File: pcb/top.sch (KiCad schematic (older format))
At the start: 12 parts, among them J11 1-MALE, J12 1-FEMALE, J13 2-MALE, J14 2-FEMALE, J15 3-MALE, J16 3-FEMALE, J17 4-MALE, J18 4-FEMALE, SW1 ACTION, SW2 ACTION, SW3 ACTION, SW4 ACTION

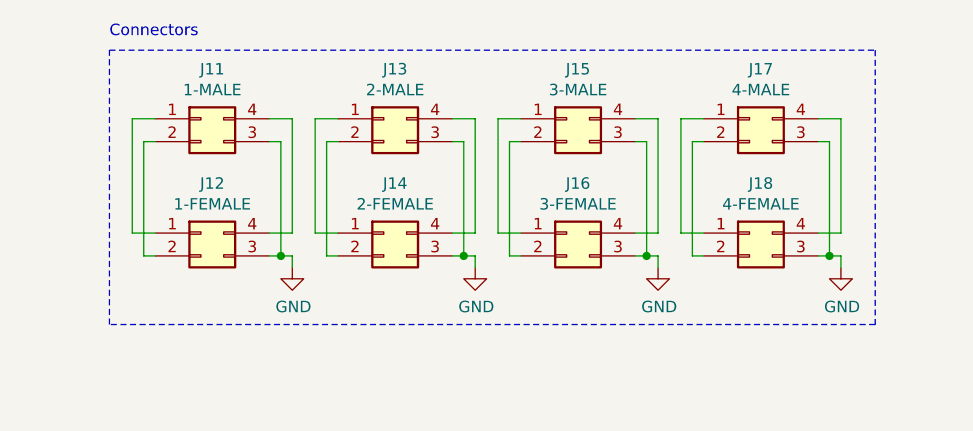
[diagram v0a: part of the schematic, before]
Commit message: Assign footprints and complete BOM
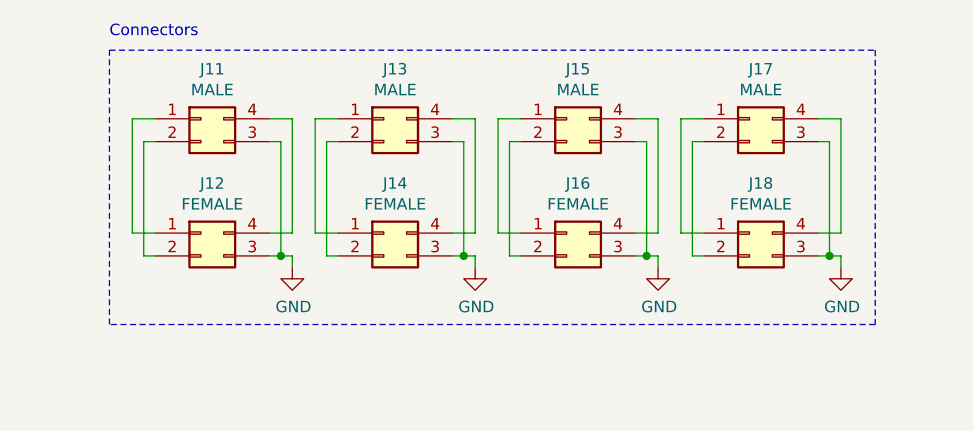
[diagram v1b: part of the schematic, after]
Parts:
- J11: value 1-MALE -> MALE; LCSC Part # (none) -> C239333; MPN (none) -> A2541WR-2x2P; Manufacturer (none) -> CJT(Changjiang Connectors)
- J12: value 1-FEMALE -> FEMALE; LCSC Part # (none) -> C239353; MPN (none) -> A2541HWR-2x2P; Manufacturer (none) -> CJT(Changjiang Connectors)
- J13: value 2-MALE -> MALE; LCSC Part # (none) -> C239333; MPN (none) -> A2541WR-2x2P; Manufacturer (none) -> CJT(Changjiang Connectors)
- J14: value 2-FEMALE -> FEMALE; LCSC Part # (none) -> C239353; MPN (none) -> A2541HWR-2x2P; Manufacturer (none) -> CJT(Changjiang Connectors)
- J15: value 3-MALE -> MALE; LCSC Part # (none) -> C239333; MPN (none) -> A2541WR-2x2P; Manufacturer (none) -> CJT(Changjiang Connectors)
- J16: value 3-FEMALE -> FEMALE; LCSC Part # (none) -> C239353; MPN (none) -> A2541HWR-2x2P; Manufacturer (none) -> CJT(Changjiang Connectors)
- J17: value 4-MALE -> MALE; LCSC Part # (none) -> C239333; MPN (none) -> A2541WR-2x2P; Manufacturer (none) -> CJT(Changjiang Connectors)
- J18: value 4-FEMALE -> FEMALE; LCSC Part # (none) -> C239353; MPN (none) -> A2541HWR-2x2P; Manufacturer (none) -> CJT(Changjiang Connectors)
- SW1, SW2, SW3, SW4: footprint (none) -> Button_Switch_SMD:SW_SPST_TL3305A; LCSC Part # (none) -> C412374; MPN (none) -> TS4560TP; Manufacturer (none) -> SHOU HAN
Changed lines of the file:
@@
 AR Path="/5C920CA4/5F6ACD6B" Ref="J11"  Part="1"
 F 0 "J11" H 3850 2317 50  0000 C CNN
-F 1 "1-MALE" H 3850 2226 50  0000 C CNN
+F 1 "MALE" H 3850 2226 50  0000 C CNN
 F 2 "Connector_PinHeader_2.54mm:PinHeader_2x02_P2.54mm_Horizontal" H 3800 2100 50  0001 C CNN
-F 3 "~" H 3800 2100 50  0001 C CNN
+F 3 "https://datasheet.lcsc.com/szlcsc/2008120037_CJT-Changjiang-Connectors-A2541WR-2x2P_C239333.pdf" H 3800 2100 50  0001 C CNN
+F 4 "C239333" H 3800 2100 50  0001 C CNN "LCSC Part #"
+F 5 "A2541WR-2x2P" H 3800 2100 50  0001 C CNN "MPN"
+F 6 "CJT(Changjiang Connectors)" H 3800 2100 50  0001 C CNN "Manufacturer"
 	1    3800 2100
 	1    0    0    -1
@@
 AR Path="/5C920CA4/5F6ACD85" Ref="J12"  Part="1"
 F 0 "J12" H 3850 2817 50  0000 C CNN
-F 1 "1-FEMALE" H 3850 2726 50  0000 C CNN
+F 1 "FEMALE" H 3850 2726 50  0000 C CNN
 F 2 "Connector_PinSocket_2.54mm:PinSocket_2x02_P2.54mm_Horizontal" H 3800 2600 50  0001 C CNN
-F 3 "~" H 3800 2600 50  0001 C CNN
+F 3 "https://datasheet.lcsc.com/szlcsc/2008120038_CJT-Changjiang-Connectors-A2541HWR-2x2P_C239353.pdf" H 3800 2600 50  0001 C CNN
+F 4 "C239353" H 3800 2600 50  0001 C CNN "LCSC Part #"
+F 5 "A2541HWR-2x2P" H 3800 2600 50  0001 C CNN "MPN"
+F 6 "CJT(Changjiang Connectors)" H 3800 2600 50  0001 C CNN "Manufacturer"
 	1    3800 2600
 	1    0    0    -1
@@
 AR Path="/5C920CA4/5F6B6610" Ref="J13"  Part="1"
 F 0 "J13" H 4650 2317 50  0000 C CNN
-F 1 "2-MALE" H 4650 2226 50  0000 C CNN
+F 1 "MALE" H 4650 2226 50  0000 C CNN
 F 2 "Connector_PinHeader_2.54mm:PinHeader_2x02_P2.54mm_Horizontal" H 4600 2100 50  0001 C CNN
-F 3 "~" H 4600 2100 50  0001 C CNN
+F 3 "https://datasheet.lcsc.com/szlcsc/2008120037_CJT-Changjiang-Connectors-A2541WR-2x2P_C239333.pdf" H 4600 2100 50  0001 C CNN
+F 4 "C239333" H 4600 2100 50  0001 C CNN "LCSC Part #"
+F 5 "A2541WR-2x2P" H 4600 2100 50  0001 C CNN "MPN"
+F 6 "CJT(Changjiang Connectors)" H 4600 2100 50  0001 C CNN "Manufacturer"
 	1    4600 2100
 	1    0    0    -1
@@
 AR Path="/5C920CA4/5F6B6626" Ref="J14"  Part="1"
 F 0 "J14" H 4650 2817 50  0000 C CNN
-F 1 "2-FEMALE" H 4650 2726 50  0000 C CNN
+F 1 "FEMALE" H 4650 2726 50  0000 C CNN
 F 2 "Connector_PinSocket_2.54mm:PinSocket_2x02_P2.54mm_Horizontal" H 4600 2600 50  0001 C CNN
-F 3 "~" H 4600 2600 50  0001 C CNN
+F 3 "https://datasheet.lcsc.com/szlcsc/2008120038_CJT-Changjiang-Connectors-A2541HWR-2x2P_C239353.pdf" H 4600 2600 50  0001 C CNN
+F 4 "C239353" H 4600 2600 50  0001 C CNN "LCSC Part #"
+F 5 "A2541HWR-2x2P" H 4600 2600 50  0001 C CNN "MPN"
+F 6 "CJT(Changjiang Connectors)" H 4600 2600 50  0001 C CNN "Manufacturer"
 	1    4600 2600
 	1    0    0    -1
@@
 AR Path="/5C920CA4/5F6B83E3" Ref="J15"  Part="1"
 F 0 "J15" H 5450 2317 50  0000 C CNN
-F 1 "3-MALE" H 5450 2226 50  0000 C CNN
+F 1 "MALE" H 5450 2226 50  0000 C CNN
 F 2 "Connector_PinHeader_2.54mm:PinHeader_2x02_P2.54mm_Horizontal" H 5400 2100 50  0001 C CNN
-F 3 "~" H 5400 2100 50  0001 C CNN
+F 3 "https://datasheet.lcsc.com/szlcsc/2008120037_CJT-Changjiang-Connectors-A2541WR-2x2P_C239333.pdf" H 5400 2100 50  0001 C CNN
+F 4 "C239333" H 5400 2100 50  0001 C CNN "LCSC Part #"
+F 5 "A2541WR-2x2P" H 5400 2100 50  0001 C CNN "MPN"
+F 6 "CJT(Changjiang Connectors)" H 5400 2100 50  0001 C CNN "Manufacturer"
 	1    5400 2100
 	1    0    0    -1
@@
 AR Path="/5C920CA4/5F6B83F9" Ref="J16"  Part="1"
 F 0 "J16" H 5450 2817 50  0000 C CNN
-F 1 "3-FEMALE" H 5450 2726 50  0000 C CNN
+F 1 "FEMALE" H 5450 2726 50  0000 C CNN
 F 2 "Connector_PinSocket_2.54mm:PinSocket_2x02_P2.54mm_Horizontal" H 5400 2600 50  0001 C CNN
-F 3 "~" H 5400 2600 50  0001 C CNN
+F 3 "https://datasheet.lcsc.com/szlcsc/2008120038_CJT-Changjiang-Connectors-A2541HWR-2x2P_C239353.pdf" H 5400 2600 50  0001 C CNN
+F 4 "C239353" H 5400 2600 50  0001 C CNN "LCSC Part #"
+F 5 "A2541HWR-2x2P" H 5400 2600 50  0001 C CNN "MPN"
+F 6 "CJT(Changjiang Connectors)" H 5400 2600 50  0001 C CNN "Manufacturer"
 	1    5400 2600
 	1    0    0    -1
@@
 AR Path="/5C920CA4/5F6BA361" Ref="J17"  Part="1"
 F 0 "J17" H 6250 2317 50  0000 C CNN
-F 1 "4-MALE" H 6250 2226 50  0000 C CNN
+F 1 "MALE" H 6250 2226 50  0000 C CNN
 F 2 "Connector_PinHeader_2.54mm:PinHeader_2x02_P2.54mm_Horizontal" H 6200 2100 50  0001 C CNN
-F 3 "~" H 6200 2100 50  0001 C CNN
+F 3 "https://datasheet.lcsc.com/szlcsc/2008120037_CJT-Changjiang-Connectors-A2541WR-2x2P_C239333.pdf" H 6200 2100 50  0001 C CNN
+F 4 "C239333" H 6200 2100 50  0001 C CNN "LCSC Part #"
+F 5 "A2541WR-2x2P" H 6200 2100 50  0001 C CNN "MPN"
+F 6 "CJT(Changjiang Connectors)" H 6200 2100 50  0001 C CNN "Manufacturer"
 	1    6200 2100
 	1    0    0    -1
@@
 AR Path="/5C920CA4/5F6BA377" Ref="J18"  Part="1"
 F 0 "J18" H 6250 2817 50  0000 C CNN
-F 1 "4-FEMALE" H 6250 2726 50  0000 C CNN
+F 1 "FEMALE" H 6250 2726 50  0000 C CNN
 F 2 "Connector_PinSocket_2.54mm:PinSocket_2x02_P2.54mm_Horizontal" H 6200 2600 50  0001 C CNN
-F 3 "~" H 6200 2600 50  0001 C CNN
+F 3 "https://datasheet.lcsc.com/szlcsc/2008120038_CJT-Changjiang-Connectors-A2541HWR-2x2P_C239353.pdf" H 6200 2600 50  0001 C CNN
+F 4 "C239353" H 6200 2600 50  0001 C CNN "LCSC Part #"
+F 5 "A2541HWR-2x2P" H 6200 2600 50  0001 C CNN "MPN"
+F 6 "CJT(Changjiang Connectors)" H 6200 2600 50  0001 C CNN "Manufacturer"
 	1    6200 2600
 	1    0    0    -1
@@
 F 0 "SW1" H 2900 4485 50  0000 C CNN
 F 1 "ACTION" H 2900 4394 50  0000 C CNN
-F 2 "" H 2900 4400 50  0001 C CNN
-F 3 "~" H 2900 4400 50  0001 C CNN
+F 2 "Button_Switch_SMD:SW_SPST_TL3305A" H 2900 4400 50  0001 C CNN
+F 3 "https://datasheet.lcsc.com/szlcsc/1912111437_SHOU-HAN-TS4560TP_C412374.pdf" H 2900 4400 50  0001 C CNN
+F 4 "C412374" H 2900 4200 50  0001 C CNN "LCSC Part #"
+F 5 "TS4560TP" H 2900 4200 50  0001 C CNN "MPN"
+F 6 "SHOU HAN" H 2900 4200 50  0001 C CNN "Manufacturer"
 	1    2900 4200
 	1    0    0    -1
@@
 F 0 "SW2" H 4400 4485 50  0000 C CNN
 F 1 "ACTION" H 4400 4394 50  0000 C CNN
-F 2 "" H 4400 4400 50  0001 C CNN
-F 3 "~" H 4400 4400 50  0001 C CNN
+F 2 "Button_Switch_SMD:SW_SPST_TL3305A" H 4400 4400 50  0001 C CNN
+F 3 "https://datasheet.lcsc.com/szlcsc/1912111437_SHOU-HAN-TS4560TP_C412374.pdf" H 4400 4400 50  0001 C CNN
+F 4 "C412374" H 4400 4200 50  0001 C CNN "LCSC Part #"
+F 5 "TS4560TP" H 4400 4200 50  0001 C CNN "MPN"
+F 6 "SHOU HAN" H 4400 4200 50  0001 C CNN "Manufacturer"
 	1    4400 4200
 	1    0    0    -1
@@
 F 0 "SW3" H 5900 4485 50  0000 C CNN
 F 1 "ACTION" H 5900 4394 50  0000 C CNN
-F 2 "" H 5900 4400 50  0001 C CNN
-F 3 "~" H 5900 4400 50  0001 C CNN
+F 2 "Button_Switch_SMD:SW_SPST_TL3305A" H 5900 4400 50  0001 C CNN
+F 3 "https://datasheet.lcsc.com/szlcsc/1912111437_SHOU-HAN-TS4560TP_C412374.pdf" H 5900 4400 50  0001 C CNN
+F 4 "C412374" H 5900 4200 50  0001 C CNN "LCSC Part #"
+F 5 "TS4560TP" H 5900 4200 50  0001 C CNN "MPN"
+F 6 "SHOU HAN" H 5900 4200 50  0001 C CNN "Manufacturer"
 	1    5900 4200
 	1    0    0    -1
@@
 F 0 "SW4" H 7400 4485 50  0000 C CNN
 F 1 "ACTION" H 7400 4394 50  0000 C CNN
-F 2 "" H 7400 4400 50  0001 C CNN
-F 3 "~" H 7400 4400 50  0001 C CNN
+F 2 "Button_Switch_SMD:SW_SPST_TL3305A" H 7400 4400 50  0001 C CNN
+F 3 "https://datasheet.lcsc.com/szlcsc/1912111437_SHOU-HAN-TS4560TP_C412374.pdf" H 7400 4400 50  0001 C CNN
+F 4 "C412374" H 7400 4200 50  0001 C CNN "LCSC Part #"
+F 5 "TS4560TP" H 7400 4200 50  0001 C CNN "MPN"
+F 6 "SHOU HAN" H 7400 4200 50  0001 C CNN "Manufacturer"
 	1    7400 4200
 	1    0    0    -1

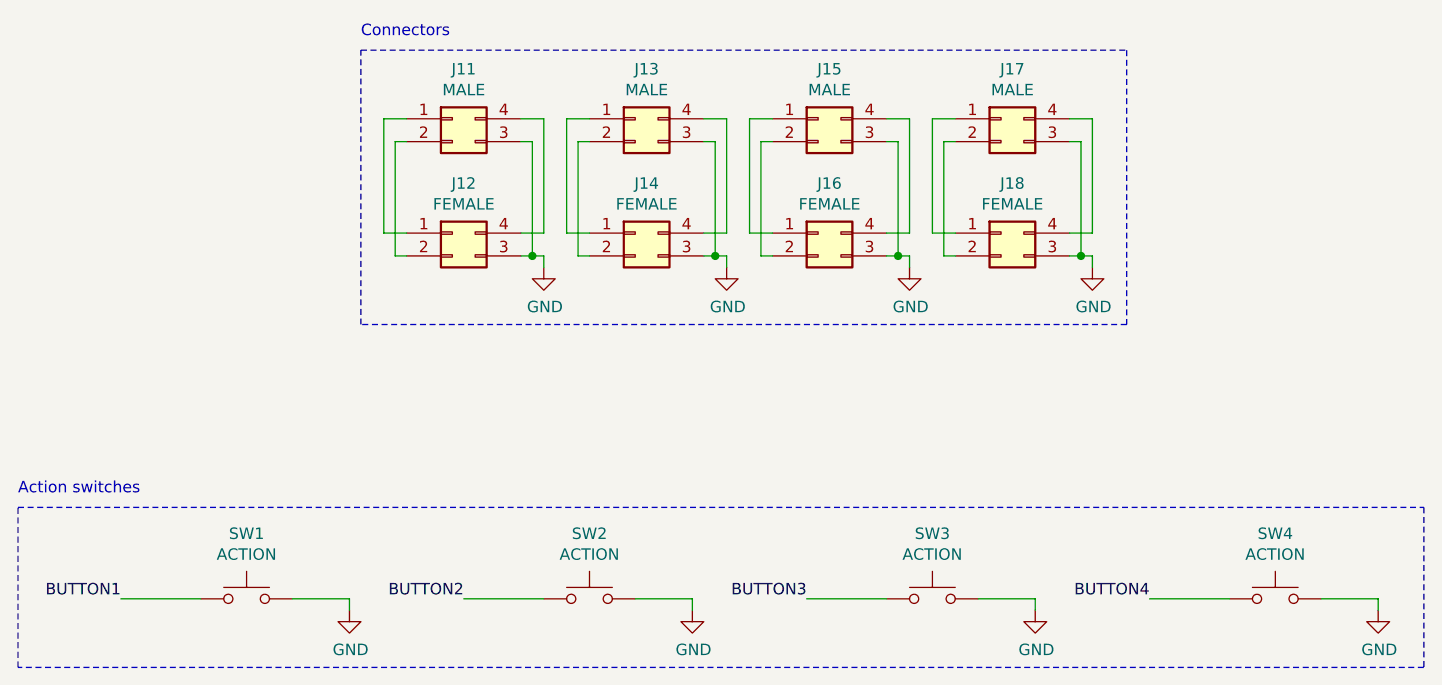
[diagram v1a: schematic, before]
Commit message: Add buzzer and clean up
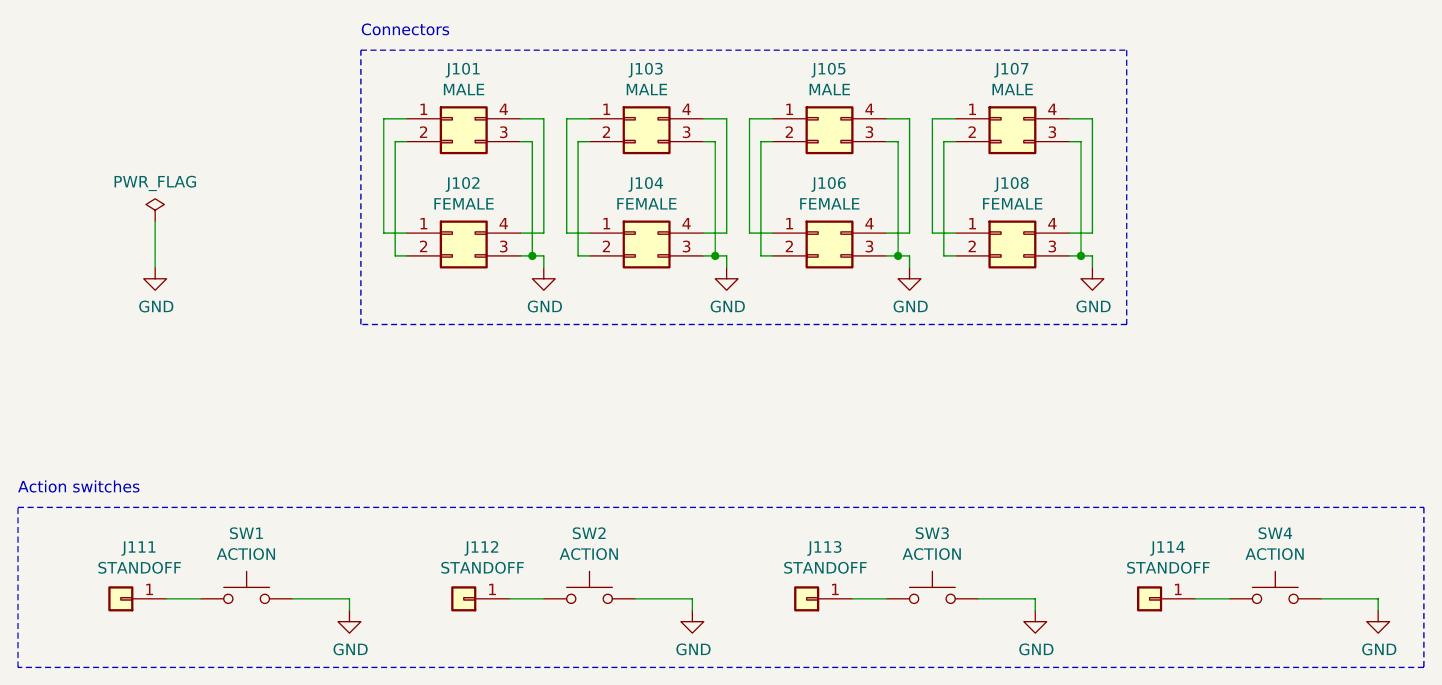
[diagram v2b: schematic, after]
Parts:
- added J111, J112, J113, J114: STANDOFF, MountingHole:MountingHole_2.2mm_M2_Pad_Via, symbol Connector_Generic:Conn_01x01
- renumbered J11 to J101, J12 to J102, J13 to J103, J14 to J104, J15 to J105, J16 to J106, J17 to J107, J18 to J108
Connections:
- net BUTTON1: no longer names the net of SW1.1
- net BUTTON1: now also J111.1 (Pin_1)
- net BUTTON2: no longer names the net of SW2.1
- net BUTTON2: now also J112.1 (Pin_1)
- net BUTTON3: no longer names the net of SW3.1
- net BUTTON3: now also J113.1 (Pin_1)
- net BUTTON4: no longer names the net of SW4.1
- net BUTTON4: now also J114.1 (Pin_1)
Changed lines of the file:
@@
 $Descr A4 11693 8268
 encoding utf-8
-Sheet 3 3
+Sheet 2 3
 Title "Top"
 Date ""
@@
 P 3800 2100
 AR Path="/5C920754/5F6ACD6B" Ref="J?"  Part="1"
-AR Path="/5C920CA4/5F6ACD6B" Ref="J11"  Part="1"
-F 0 "J11" H 3850 2317 50  0000 C CNN
+AR Path="/5C920CA4/5F6ACD6B" Ref="J101"  Part="1"
+F 0 "J101" H 3850 2317 50  0000 C CNN
 F 1 "MALE" H 3850 2226 50  0000 C CNN
 F 2 "Connector_PinHeader_2.54mm:PinHeader_2x02_P2.54mm_Horizontal" H 3800 2100 50  0001 C CNN
@@
 P 3800 2600
 AR Path="/5C920754/5F6ACD85" Ref="J?"  Part="1"
-AR Path="/5C920CA4/5F6ACD85" Ref="J12"  Part="1"
-F 0 "J12" H 3850 2817 50  0000 C CNN
+AR Path="/5C920CA4/5F6ACD85" Ref="J102"  Part="1"
+F 0 "J102" H 3850 2817 50  0000 C CNN
 F 1 "FEMALE" H 3850 2726 50  0000 C CNN
 F 2 "Connector_PinSocket_2.54mm:PinSocket_2x02_P2.54mm_Horizontal" H 3800 2600 50  0001 C CNN
@@
 P 4600 2100
 AR Path="/5C920754/5F6B6610" Ref="J?"  Part="1"
-AR Path="/5C920CA4/5F6B6610" Ref="J13"  Part="1"
-F 0 "J13" H 4650 2317 50  0000 C CNN
+AR Path="/5C920CA4/5F6B6610" Ref="J103"  Part="1"
+F 0 "J103" H 4650 2317 50  0000 C CNN
 F 1 "MALE" H 4650 2226 50  0000 C CNN
 F 2 "Connector_PinHeader_2.54mm:PinHeader_2x02_P2.54mm_Horizontal" H 4600 2100 50  0001 C CNN
@@
 P 4600 2600
 AR Path="/5C920754/5F6B6626" Ref="J?"  Part="1"
-AR Path="/5C920CA4/5F6B6626" Ref="J14"  Part="1"
-F 0 "J14" H 4650 2817 50  0000 C CNN
+AR Path="/5C920CA4/5F6B6626" Ref="J104"  Part="1"
+F 0 "J104" H 4650 2817 50  0000 C CNN
 F 1 "FEMALE" H 4650 2726 50  0000 C CNN
 F 2 "Connector_PinSocket_2.54mm:PinSocket_2x02_P2.54mm_Horizontal" H 4600 2600 50  0001 C CNN
@@
 P 5400 2100
 AR Path="/5C920754/5F6B83E3" Ref="J?"  Part="1"
-AR Path="/5C920CA4/5F6B83E3" Ref="J15"  Part="1"
-F 0 "J15" H 5450 2317 50  0000 C CNN
+AR Path="/5C920CA4/5F6B83E3" Ref="J105"  Part="1"
+F 0 "J105" H 5450 2317 50  0000 C CNN
 F 1 "MALE" H 5450 2226 50  0000 C CNN
 F 2 "Connector_PinHeader_2.54mm:PinHeader_2x02_P2.54mm_Horizontal" H 5400 2100 50  0001 C CNN
@@
 P 5400 2600
 AR Path="/5C920754/5F6B83F9" Ref="J?"  Part="1"
-AR Path="/5C920CA4/5F6B83F9" Ref="J16"  Part="1"
-F 0 "J16" H 5450 2817 50  0000 C CNN
+AR Path="/5C920CA4/5F6B83F9" Ref="J106"  Part="1"
+F 0 "J106" H 5450 2817 50  0000 C CNN
 F 1 "FEMALE" H 5450 2726 50  0000 C CNN
 F 2 "Connector_PinSocket_2.54mm:PinSocket_2x02_P2.54mm_Horizontal" H 5400 2600 50  0001 C CNN
@@
 P 6200 2100
 AR Path="/5C920754/5F6BA361" Ref="J?"  Part="1"
-AR Path="/5C920CA4/5F6BA361" Ref="J17"  Part="1"
-F 0 "J17" H 6250 2317 50  0000 C CNN
+AR Path="/5C920CA4/5F6BA361" Ref="J107"  Part="1"
+F 0 "J107" H 6250 2317 50  0000 C CNN
 F 1 "MALE" H 6250 2226 50  0000 C CNN
 F 2 "Connector_PinHeader_2.54mm:PinHeader_2x02_P2.54mm_Horizontal" H 6200 2100 50  0001 C CNN
@@
 P 6200 2600
 AR Path="/5C920754/5F6BA377" Ref="J?"  Part="1"
-AR Path="/5C920CA4/5F6BA377" Ref="J18"  Part="1"
-F 0 "J18" H 6250 2817 50  0000 C CNN
+AR Path="/5C920CA4/5F6BA377" Ref="J108"  Part="1"
+F 0 "J108" H 6250 2817 50  0000 C CNN
 F 1 "FEMALE" H 6250 2726 50  0000 C CNN
 F 2 "Connector_PinSocket_2.54mm:PinSocket_2x02_P2.54mm_Horizontal" H 6200 2600 50  0001 C CNN
@@
 Connection ~ 6550 2700
 Wire Wire Line
-	2350 4200 2700 4200
+	2550 4200 2700 4200
 Wire Wire Line
 	3100 4200 3350 4200
@@
 	1    0    0    -1
 $EndComp
-Text Label 2350 4200 2    50   ~ 0
-BUTTON1
 Wire Notes Line
 	3400 1800 6750 1800
@@
 Action switches
 Wire Wire Line
-	3850 4200 4200 4200
+	4050 4200 4200 4200
 Wire Wire Line
 	4600 4200 4850 4200
-$Comp
-L power:GND #PWR?
-U 1 1 5F85B221
-P 4850 4250
-AR Path="/5C920754/5F85B221" Ref="#PWR?"  Part="1"
-AR Path="/5C920CA4/5F85B221" Ref="#PWR01"  Part="1"
-F 0 "#PWR01" H 4850 4000 50  0001 C CNN
-F 1 "GND" H 4855 4077 50  0000 C CNN
-F 2 "" H 4850 4250 50  0001 C CNN
-F 3 "" H 4850 4250 50  0001 C CNN
-	1    4850 4250
-	1    0    0    -1
-$EndComp
 Wire Wire Line
 	4850 4200 4850 4250
@@
 	1    0    0    -1
 $EndComp
-Text Label 3850 4200 2    50   ~ 0
-BUTTON2
-Wire Wire Line
-	5350 4200 5700 4200
+Wire Wire Line
+	5550 4200 5700 4200
 Wire Wire Line
 	6100 4200 6350 4200
@@
 	1    0    0    -1
 $EndComp
-Text Label 5350 4200 2    50   ~ 0
-BUTTON3
-Wire Wire Line
-	6850 4200 7200 4200
+Wire Wire Line
+	7050 4200 7200 4200
 Wire Wire Line
 	7600 4200 7850 4200
@@
 	1    0    0    -1
 $EndComp
-Text Label 6850 4200 2    50   ~ 0
-BUTTON4
 Wire Notes Line
 	1900 3800 8050 3800
@@
 Wire Notes Line
 	8050 4500 1900 4500
+$Comp
+L power:GND #PWR?
+U 1 1 5F8EB7F9
+P 4850 4250
+AR Path="/5C920754/5F8EB7F9" Ref="#PWR?"  Part="1"
+AR Path="/5C920CA4/5F8EB7F9" Ref="#PWR0130"  Part="1"
+F 0 "#PWR0130" H 4850 4000 50  0001 C CNN
+F 1 "GND" H 4855 4077 50  0000 C CNN
+F 2 "" H 4850 4250 50  0001 C CNN
+F 3 "" H 4850 4250 50  0001 C CNN
+	1    4850 4250
+	1    0    0    -1
+$EndComp
+$Comp
+L Connector_Generic:Conn_01x01 J111
+U 1 1 5F8ECF05
+P 2350 4200
+F 0 "J111" H 2268 3975 50  0000 C CNN
+F 1 "STANDOFF" H 2268 4066 50  0000 C CNN
+F 2 "MountingHole:MountingHole_2.2mm_M2_Pad_Via" H 2350 4200 50  0001 C CNN
+F 3 "~" H 2350 4200 50  0001 C CNN
+	1    2350 4200
+	-1   0    0    1
+$EndComp
+$Comp
+L Connector_Generic:Conn_01x01 J112
+U 1 1 5F8EF776
+P 3850 4200
+F 0 "J112" H 3768 3975 50  0000 C CNN
+F 1 "STANDOFF" H 3768 4066 50  0000 C CNN
+F 2 "MountingHole:MountingHole_2.2mm_M2_Pad_Via" H 3850 4200 50  0001 C CNN
+F 3 "~" H 3850 4200 50  0001 C CNN
+	1    3850 4200
+	-1   0    0    1
+$EndComp
+$Comp
+L Connector_Generic:Conn_01x01 J113
+U 1 1 5F8F0A30
+P 5350 4200
+F 0 "J113" H 5268 3975 50  0000 C CNN
+F 1 "STANDOFF" H 5268 4066 50  0000 C CNN
+F 2 "MountingHole:MountingHole_2.2mm_M2_Pad_Via" H 5350 4200 50  0001 C CNN
+F 3 "~" H 5350 4200 50  0001 C CNN
+	1    5350 4200
+	-1   0    0    1
+$EndComp
+$Comp
+L Connector_Generic:Conn_01x01 J114
+U 1 1 5F8F0B43
+P 6850 4200
+F 0 "J114" H 6768 3975 50  0000 C CNN
+F 1 "STANDOFF" H 6768 4066 50  0000 C CNN
+F 2 "MountingHole:MountingHole_2.2mm_M2_Pad_Via" H 6850 4200 50  0001 C CNN
+F 3 "~" H 6850 4200 50  0001 C CNN
+	1    6850 4200
+	-1   0    0    1
+$EndComp
+$Comp
+L power:GND #PWR0131
+U 1 1 5FA30673
+P 2500 2750
+F 0 "#PWR0131" H 2500 2500 50  0001 C CNN
+F 1 "GND" H 2505 2577 50  0000 C CNN
+F 2 "" H 2500 2750 50  0001 C CNN
+F 3 "" H 2500 2750 50  0001 C CNN
+	1    2500 2750
+	1    0    0    -1
+$EndComp
+$Comp
+L power:PWR_FLAG #FLG0103
+U 1 1 5FA30DFE
+P 2500 2550
+F 0 "#FLG0103" H 2500 2625 50  0001 C CNN
+F 1 "PWR_FLAG" H 2500 2723 50  0000 C CNN
+F 2 "" H 2500 2550 50  0001 C CNN
+F 3 "~" H 2500 2550 50  0001 C CNN
+	1    2500 2550
+	1    0    0    -1
+$EndComp
+Wire Wire Line
+	2500 2550 2500 2750
 $EndSCHEMATC
